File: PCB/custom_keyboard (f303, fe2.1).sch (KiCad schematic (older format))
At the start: 424 parts, among them IC1 FE2.1, J2 Conn_01x03_Male, J5 AVR-ISP-6, Q1 DTC123J, SW1 SW_Push, U1 24LC02BT-I/SN, U10 PRTR5V0U2X, U11 XC6206P332MR, U12 74LVC1G34, U13 XC6206P332MR, U2 PRTR5V0U2X, U3 PRTR5V0U2X, U4 PRTR5V0U2X, U5 PRTR5V0U2X, U6 PRTR5V0U2X, U7 PRTR5V0U2X, U8 PRTR5V0U2X, U9 STM32F303CBT6, Y1 8MHz, Y2 32.768KHz, Y3 12MHz

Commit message: Drew outlines for case
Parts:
- removed H2, H5: Hole, MountingHole:MountingHole_3.2mm_M3_Pad, symbol Mechanical:MountingHole_Pad
- J2: footprint Connector_JST:JST_GH_SM03B-GHS-TB_1x03-1MP_P1.25mm_Horizontal -> Connector_JST:JST_SH_SM03B-SRSS-TB_1x03-1MP_P1.00mm_Horizontal
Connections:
- net KEYBOARD_D+: now also R44.1, U9.33 (PA12)
- net KEYBOARD_D-: now also R43.1, U9.32 (PA11)
- net D-: now reaches R3.2, U3.3 (IO2), USB5.5 (DN2), USB5.7 (DN1)
- net D-: now also R2.1, R20.1, R25.1, R31.1, R37.1, R46.1, U10.3 (IO2), U2.3 (IO2), U4.3 (IO2), U5.3 (IO2), U6.3 (IO2), U7.3 (IO2), USB1.5 (DN2), USB1.7 (DN1), USB2.5 (DN2), USB2.7 (DN1), USB3.2 (D-), USB4.2 (D-), USB6.2 (D-), USB7.5 (DN2), USB7.7 (DN1)
- net D+: now reaches R6.2, U3.2 (IO1), USB5.6 (DP1), USB5.8 (DP2)
- net D+: now also R19.1, R24.1, R33.1, R34.1, R4.1, R45.1, U10.2 (IO1), U2.2 (IO1), U4.2 (IO1), U5.2 (IO1), U6.2 (IO1), U7.2 (IO1), USB1.6 (DP1), USB1.8 (DP2), USB2.6 (DP1), USB2.8 (DP2), USB3.3 (D+), USB4.3 (D+), USB6.3 (D+), USB7.6 (DP1), USB7.8 (DP2)
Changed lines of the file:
@@
 	0    -1   -1   0
 $EndComp
-Text GLabel 7550 18650 2    50   Input ~ 0
-KEYBOARD_D+
 Text GLabel 7550 18550 2    50   Input ~ 0
 KEYBOARD_D-
@@
 F 0 "J2" H 7108 16581 50  0000 C CNN
 F 1 "Conn_01x03_Male" H 7108 16490 50  0000 R CNN
-F 2 "Connector_JST:JST_GH_SM03B-GHS-TB_1x03-1MP_P1.25mm_Horizontal" H 7000 16300 50  0001 C CNN
+F 2 "Connector_JST:JST_SH_SM03B-SRSS-TB_1x03-1MP_P1.00mm_Horizontal" H 7000 16300 50  0001 C CNN
 F 3 "~" H 7000 16300 50  0001 C CNN
 	1    7000 16300
@@
 $EndComp
 $Comp
-L Mechanical:MountingHole_Pad H5
-U 1 1 6FB1C97B
-P 14550 21250
-F 0 "H5" H 14650 21299 50  0000 L CNN
-F 1 "Hole" H 14650 21208 50  0000 L CNN
-F 2 "MountingHole:MountingHole_3.2mm_M3_Pad" H 14550 21250 50  0001 C CNN
-F 3 "~" H 14550 21250 50  0001 C CNN
-	1    14550 21250
-	1    0    0    -1
-$EndComp
-$Comp
 L Mechanical:MountingHole_Pad H6
 U 1 1 6FB1CEC9
@@
 	14150 21450 14150 21350
 Wire Wire Line
-	14550 21350 14550 21450
-Wire Wire Line
 	14950 21350 14950 21450
 $Comp
@@
 $EndComp
 $Comp
-L Mechanical:MountingHole_Pad H2
-U 1 1 72E561AB
-P 13350 21250
-F 0 "H2" H 13450 21299 50  0000 L CNN
-F 1 "Hole" H 13450 21208 50  0000 L CNN
-F 2 "MountingHole:MountingHole_3.2mm_M3_Pad" H 13350 21250 50  0001 C CNN
-F 3 "~" H 13350 21250 50  0001 C CNN
-	1    13350 21250
-	1    0    0    -1
-$EndComp
-$Comp
 L Mechanical:MountingHole_Pad H3
 U 1 1 72E561B5
@@
 	12950 21450 12950 21350
 Wire Wire Line
-	13350 21350 13350 21450
-Wire Wire Line
 	13750 21350 13750 21450
-Wire Wire Line
-	12950 21450 13350 21450
 Connection ~ 14950 21450
-Connection ~ 13350 21450
-Wire Wire Line
-	13350 21450 13750 21450
 Connection ~ 13750 21450
 Wire Wire Line
@@
 Connection ~ 14150 21450
 Wire Wire Line
-	14150 21450 14550 21450
-Connection ~ 14550 21450
-Wire Wire Line
-	14550 21450 14950 21450
-Wire Wire Line
 	28050 3850 27950 3850
 Connection ~ 27950 3850
@@
 Wire Wire Line
 	10900 13200 10900 13500
+Text GLabel 22650 16250 1    50   Input ~ 0
+D+
+Text GLabel 22650 16350 3    50   Input ~ 0
+D-
+Text GLabel 22650 14300 3    50   Input ~ 0
+D-
+Text GLabel 22650 12250 3    50   Input ~ 0
+D-
+Text GLabel 22650 14200 1    50   Input ~ 0
+D+
+Text GLabel 22650 12150 1    50   Input ~ 0
+D+
+Text GLabel 26900 12300 1    50   Input ~ 0
+D-
+Text GLabel 26900 12400 3    50   Input ~ 0
+D+
+Text GLabel 26850 14850 3    50   Input ~ 0
+D+
+Text GLabel 26850 17300 3    50   Input ~ 0
+D+
+Text GLabel 26850 14750 1    50   Input ~ 0
+D-
+Text GLabel 26850 17200 1    50   Input ~ 0
+D-
+Text GLabel 14600 11950 3    50   Input ~ 0
+D+
+Text GLabel 14600 11850 1    50   Input ~ 0
+D-
+Text GLabel 7550 18650 2    50   Input ~ 0
+KEYBOARD_D+
+Text GLabel 7050 18650 3    50   Input ~ 0
+KEYBOARD_D+
+Text GLabel 7100 18550 1    50   Input ~ 0
+KEYBOARD_D-
+Wire Wire Line
+	12950 21450 13750 21450
+Wire Wire Line
+	14150 21450 14950 21450
 $EndSCHEMATC

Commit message: Draft 1-2
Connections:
- net KEYBOARD_D+: no longer R44.1, U9.33 (PA12)
- net KEYBOARD_D-: no longer R43.1, U9.32 (PA11)
- removed net D+: R19.1, R24.1, R33.1, R34.1, R4.1, R45.1, R6.2, U10.2 (IO1), U2.2 (IO1), U3.2 (IO1), U4.2 (IO1), U5.2 (IO1), U6.2 (IO1), U7.2 (IO1), USB1.6 (DP1), USB1.8 (DP2), USB2.6 (DP1), USB2.8 (DP2), USB3.3 (D+), USB4.3 (D+), USB5.6 (DP1), USB5.8 (DP2), USB6.3 (D+), USB7.6 (DP1), USB7.8 (DP2)
- removed net D-: R2.1, R20.1, R25.1, R3.2, R31.1, R37.1, R46.1, U10.3 (IO2), U2.3 (IO2), U3.3 (IO2), U4.3 (IO2), U5.3 (IO2), U6.3 (IO2), U7.3 (IO2), USB1.5 (DN2), USB1.7 (DN1), USB2.5 (DN2), USB2.7 (DN1), USB3.2 (D-), USB4.2 (D-), USB5.5 (DN2), USB5.7 (DN1), USB6.2 (D-), USB7.5 (DN2), USB7.7 (DN1)
- new net: R3.2, U3.3 (IO2), USB5.5 (DN2), USB5.7 (DN1)
- new net: R6.2, U3.2 (IO1), USB5.6 (DP1), USB5.8 (DP2)
- new net: R19.1, U4.2 (IO1), USB7.6 (DP1), USB7.8 (DP2)
- new net: R20.1, U4.3 (IO2), USB7.5 (DN2), USB7.7 (DN1)
- new net: R33.1, U6.2 (IO1), USB2.6 (DP1), USB2.8 (DP2)
- new net: R31.1, U6.3 (IO2), USB2.5 (DN2), USB2.7 (DN1)
- new net: R24.1, U5.2 (IO1), USB6.3 (D+)
- new net: R25.1, U5.3 (IO2), USB6.2 (D-)
- new net: R34.1, U7.2 (IO1), USB3.3 (D+)
- new net: R37.1, U7.3 (IO2), USB3.2 (D-)
- new net: R45.1, U10.2 (IO1), USB4.3 (D+)
- new net: R46.1, U10.3 (IO2), USB4.2 (D-)
- new net: R43.1, U9.32 (PA11)
- new net: R44.1, U9.33 (PA12)
- new net: R2.1, U2.3 (IO2), USB1.5 (DN2), USB1.7 (DN1)
- new net: R4.1, U2.2 (IO1), USB1.6 (DP1), USB1.8 (DP2)
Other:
- note added: "USB C Outputs"
- note removed: "USB C Outputs (5-7)"
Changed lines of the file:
@@
 Text GLabel 4250 3850 2    50   Input ~ 0
 ROT1_COL
-Text Notes 4550 3300 0    315  ~ 0
+Text Notes 4650 3200 0    315  ~ 0
 0
-Text Notes 6350 3300 0    315  ~ 0
+Text Notes 6100 3250 0    315  ~ 0
 1
-Text Notes 7700 3300 0    315  ~ 0
+Text Notes 7500 3250 0    315  ~ 0
 2
-Text Notes 3500 4050 0    315  ~ 0
-0
-Text Notes 3500 5050 0    315  ~ 0
+Text Notes 3350 5000 0    315  ~ 0
 1
-Text Notes 3500 6050 0    315  ~ 0
+Text Notes 3350 6000 0    315  ~ 0
 2
-Text Notes 3500 7050 0    315  ~ 0
+Text Notes 3350 7000 0    315  ~ 0
 3
-Text Notes 3500 8050 0    315  ~ 0
+Text Notes 3350 8000 0    315  ~ 0
 4
 Wire Wire Line
@@
 Text GLabel 8350 3100 1    50   Input ~ 0
 COL3
-Text Notes 11850 3300 0    315  ~ 0
+Text Notes 11750 3250 0    315  ~ 0
 5
-Text Notes 10450 3300 0    315  ~ 0
+Text Notes 10300 3250 0    315  ~ 0
 4
-Text Notes 9100 3300 0    315  ~ 0
+Text Notes 8900 3250 0    315  ~ 0
 3
 $Comp
@@
 Wire Wire Line
 	5300 4750 5300 4850
-Text Notes 13250 3300 0    315  ~ 0
+Text Notes 13100 3250 0    315  ~ 0
 6
-Text Notes 14700 3300 0    315  ~ 0
+Text Notes 14500 3250 0    315  ~ 0
 7
-Text Notes 16100 3300 0    315  ~ 0
+Text Notes 15900 3250 0    315  ~ 0
 8
-Text Notes 17450 3300 0    315  ~ 0
+Text Notes 17300 3250 0    315  ~ 0
 9
-Text Notes 18700 3300 0    315  ~ 0
+Text Notes 18550 3250 0    315  ~ 0
 10
-Text Notes 20100 3300 0    315  ~ 0
+Text Notes 20000 3250 0    315  ~ 0
 11
-Text Notes 21500 3300 0    315  ~ 0
+Text Notes 21350 3250 0    315  ~ 0
 12
-Text Notes 22900 3300 0    315  ~ 0
+Text Notes 22750 3250 0    315  ~ 0
 13
-Text Notes 24300 3300 0    315  ~ 0
+Text Notes 24150 3250 0    315  ~ 0
 14
 Text GLabel 16750 3100 1    50   Input ~ 0
@@
 Wire Wire Line
 	28550 4150 28550 4250
-Text Notes 28200 3300 0    315  ~ 0
+Text Notes 28400 3200 0    315  ~ 0
 17
-Text Notes 27100 3300 0    315  ~ 0
+Text Notes 26950 3250 0    315  ~ 0
 16
-Text Notes 25700 3300 0    315  ~ 0
+Text Notes 25550 3250 0    315  ~ 0
 15
 Text GLabel 28050 3850 2    50   Input ~ 0
@@
 Wire Wire Line
 	4150 7650 4150 6650
-Text Notes 3500 9050 0    315  ~ 0
+Text Notes 3350 9000 0    315  ~ 0
 5
 Text GLabel 4050 4850 0    50   Input ~ 0
@@
 Text GLabel 28350 17200 2    50   Input ~ 0
 HUB_PORT7_D-
-Text Notes 28300 11100 2    118  ~ 24
-USB C Outputs (5-7)
+Text Notes 28100 11150 2    118  ~ 24
+USB C Outputs
 Text Notes 21350 11500 0    79   ~ 0
 USB Output 3\n
@@
 Wire Wire Line
 	10900 13200 10900 13500
-Text GLabel 22650 16250 1    50   Input ~ 0
-D+
-Text GLabel 22650 16350 3    50   Input ~ 0
-D-
-Text GLabel 22650 14300 3    50   Input ~ 0
-D-
-Text GLabel 22650 12250 3    50   Input ~ 0
-D-
-Text GLabel 22650 14200 1    50   Input ~ 0
-D+
-Text GLabel 22650 12150 1    50   Input ~ 0
-D+
-Text GLabel 26900 12300 1    50   Input ~ 0
-D-
-Text GLabel 26900 12400 3    50   Input ~ 0
-D+
-Text GLabel 26850 14850 3    50   Input ~ 0
-D+
-Text GLabel 26850 17300 3    50   Input ~ 0
-D+
-Text GLabel 26850 14750 1    50   Input ~ 0
-D-
-Text GLabel 26850 17200 1    50   Input ~ 0
-D-
-Text GLabel 14600 11950 3    50   Input ~ 0
-D+
-Text GLabel 14600 11850 1    50   Input ~ 0
-D-
 Text GLabel 7550 18650 2    50   Input ~ 0
 KEYBOARD_D+
-Text GLabel 7050 18650 3    50   Input ~ 0
-KEYBOARD_D+
-Text GLabel 7100 18550 1    50   Input ~ 0
-KEYBOARD_D-
 Wire Wire Line
 	12950 21450 13750 21450
@@
 Wire Wire Line
 	9600 17200 9600 17000
+Text Notes 3350 4000 0    315  ~ 0
+0
 $EndSCHEMATC

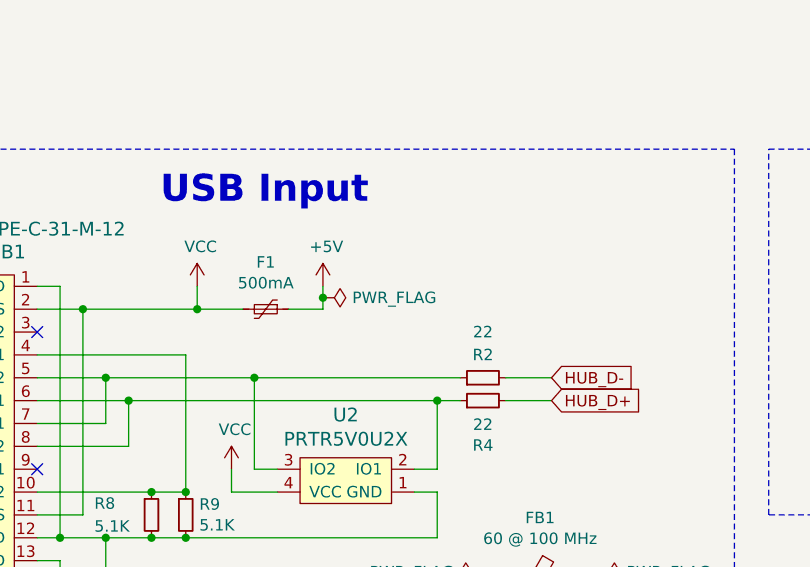
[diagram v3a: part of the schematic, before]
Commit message: Added a ferrite bead
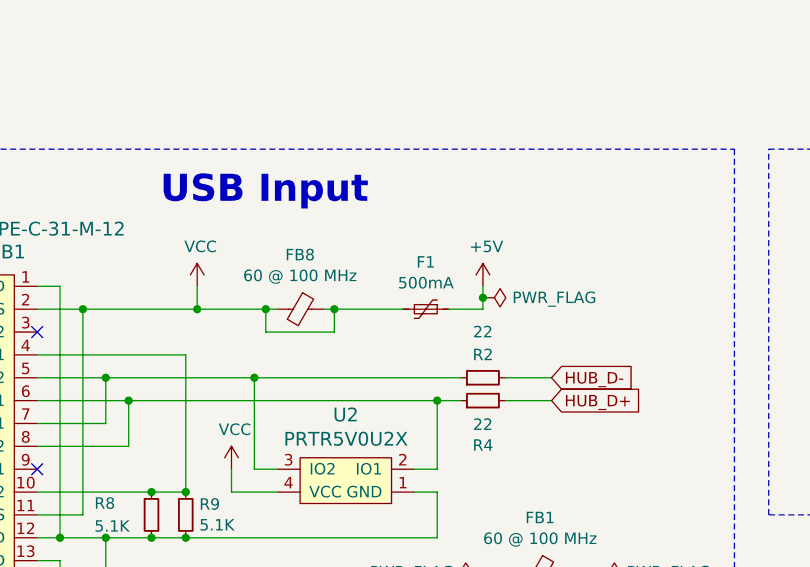
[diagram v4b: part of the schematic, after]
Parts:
- added FB8: 60 @ 100 MHz, Inductor_SMD:L_0805_2012Metric, symbol Device:Ferrite_Bead_Small
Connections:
- net +5V: now also FB8.1, FB8.2
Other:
- moved on the sheet: F1
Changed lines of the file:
@@
 	13950 12550 14150 12550
 $Comp
-L Device:Polyfuse_Small F1
-U 1 1 65C14F91
-P 14850 11550
-F 0 "F1" V 14645 11550 50  0000 C CNN
-F 1 "500mA" V 14736 11550 50  0000 C CNN
-F 2 "Fuse:Fuse_1206_3216Metric" H 14900 11350 50  0001 L CNN
-F 3 "~" H 14850 11550 50  0001 C CNN
-	1    14850 11550
-	0    1    1    0
-$EndComp
-$Comp
 L power:VCC #PWR091
 U 1 1 65C15E5C
@@
 L power:+5V #PWR092
 U 1 1 65C1A24C
-P 15100 11450
-F 0 "#PWR092" H 15100 11300 50  0001 C CNN
-F 1 "+5V" H 15115 11623 50  0000 C CNN
-F 2 "" H 15100 11450 50  0001 C CNN
-F 3 "" H 15100 11450 50  0001 C CNN
-	1    15100 11450
+P 15800 11450
+F 0 "#PWR092" H 15800 11300 50  0001 C CNN
+F 1 "+5V" H 15815 11623 50  0000 C CNN
+F 2 "" H 15800 11450 50  0001 C CNN
+F 3 "" H 15800 11450 50  0001 C CNN
+	1    15800 11450
 	1    0    0    -1
 $EndComp
-Wire Wire Line
-	15100 11550 14950 11550
-Wire Wire Line
-	14750 11550 14550 11550
 Connection ~ 14550 11550
 Wire Wire Line
@@
 Wire Wire Line
 	14550 11450 14550 11550
-$Comp
-L power:PWR_FLAG #FLG01
-U 1 1 E54A8F9E
-P 15100 11500
-F 0 "#FLG01" H 15100 11575 50  0001 C CNN
-F 1 "PWR_FLAG" V 15100 11628 50  0000 L CNN
-F 2 "" H 15100 11500 50  0001 C CNN
-F 3 "~" H 15100 11500 50  0001 C CNN
-	1    15100 11500
-	0    1    1    0
-$EndComp
-Wire Wire Line
-	15100 11450 15100 11500
-Wire Wire Line
-	15100 11500 15100 11550
-Connection ~ 15100 11500
 Wire Wire Line
 	17150 18650 17150 18850
@@
 Text Notes 3350 4000 0    315  ~ 0
 0
+Connection ~ 15800 11500
+Wire Wire Line
+	15800 11500 15800 11550
+Wire Wire Line
+	15800 11450 15800 11500
+$Comp
+L power:PWR_FLAG #FLG01
+U 1 1 E54A8F9E
+P 15800 11500
+F 0 "#FLG01" H 15800 11575 50  0001 C CNN
+F 1 "PWR_FLAG" V 15800 11628 50  0000 L CNN
+F 2 "" H 15800 11500 50  0001 C CNN
+F 3 "~" H 15800 11500 50  0001 C CNN
+	1    15800 11500
+	0    1    1    0
+$EndComp
+Wire Wire Line
+	15800 11550 15650 11550
+$Comp
+L Device:Ferrite_Bead_Small FB8
+U 1 1 6235F25C
+P 15000 11550
+F 0 "FB8" V 14763 11550 50  0000 C CNN
+F 1 "60 @ 100 MHz" V 14854 11550 50  0000 C CNN
+F 2 "Inductor_SMD:L_0805_2012Metric" V 14930 11550 50  0001 C CNN
+F 3 "~" H 15000 11550 50  0001 C CNN
+	1    15000 11550
+	0    1    1    0
+$EndComp
+$Comp
+L Device:Polyfuse_Small F1
+U 1 1 65C14F91
+P 15550 11550
+F 0 "F1" V 15345 11550 50  0000 C CNN
+F 1 "500mA" V 15436 11550 50  0000 C CNN
+F 2 "Fuse:Fuse_1206_3216Metric" H 15600 11350 50  0001 L CNN
+F 3 "~" H 15550 11550 50  0001 C CNN
+	1    15550 11550
+	0    1    1    0
+$EndComp
+Wire Wire Line
+	15100 11550 15150 11550
+Wire Wire Line
+	14550 11550 14850 11550
+Wire Wire Line
+	14850 11550 14850 11650
+Wire Wire Line
+	14850 11650 15150 11650
+Wire Wire Line
+	15150 11650 15150 11550
+Connection ~ 14850 11550
+Wire Wire Line
+	14850 11550 14900 11550
+Connection ~ 15150 11550
+Wire Wire Line
+	15150 11550 15450 11550
 $EndSCHEMATC

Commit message: Updated files, prepped for review
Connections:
- net KEYBOARD_D+: now also R44.1, U9.33 (PA12)
- net KEYBOARD_D-: now also R43.1, U9.32 (PA11)
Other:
- moved on the sheet: R42, R43, R44
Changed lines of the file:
@@
 L Device:R_Small R44
 U 1 1 83FFF6BA
-P 7250 18650
-F 0 "R44" V 7150 18750 50  0000 C CNN
-F 1 "22" V 7150 18550 50  0000 C CNN
-F 2 "Resistor_SMD:R_0805_2012Metric" H 7250 18650 50  0001 C CNN
-F 3 "~" H 7250 18650 50  0001 C CNN
-	1    7250 18650
-	0    -1   -1   0
+P 10600 17100
+F 0 "R44" V 10400 17100 50  0000 C CNN
+F 1 "22" V 10500 17100 50  0000 C CNN
+F 2 "Resistor_SMD:R_0805_2012Metric" H 10600 17100 50  0001 C CNN
+F 3 "~" H 10600 17100 50  0001 C CNN
+	1    10600 17100
+	0    -1   1    0
 $EndComp
 $Comp
 L Device:R_Small R43
 U 1 1 840036CC
-P 7250 18550
-F 0 "R43" V 7350 18650 50  0000 C CNN
-F 1 "22" V 7350 18450 50  0000 C CNN
-F 2 "Resistor_SMD:R_0805_2012Metric" H 7250 18550 50  0001 C CNN
-F 3 "~" H 7250 18550 50  0001 C CNN
-	1    7250 18550
+P 9400 17100
+F 0 "R43" V 9600 17100 50  0000 C CNN
+F 1 "22" V 9500 17100 50  0000 C CNN
+F 2 "Resistor_SMD:R_0805_2012Metric" H 9400 17100 50  0001 C CNN
+F 3 "~" H 9400 17100 50  0001 C CNN
+	1    9400 17100
 	0    -1   -1   0
 $EndComp
-Text GLabel 7550 18550 2    50   Input ~ 0
+Text GLabel 7350 18550 2    50   Input ~ 0
 KEYBOARD_D-
 Wire Wire Line
-	7450 18450 7450 18650
-Connection ~ 7450 18650
+	7250 18450 7250 18650
+Connection ~ 7250 18650
 $Comp
 L Device:R_Small R42
 U 1 1 8482A4BE
-P 7450 18350
-F 0 "R42" H 7509 18396 50  0000 L CNN
-F 1 "1.5k" H 7509 18305 50  0000 L CNN
-F 2 "Resistor_SMD:R_0805_2012Metric" H 7450 18350 50  0001 C CNN
-F 3 "~" H 7450 18350 50  0001 C CNN
-	1    7450 18350
+P 7250 18350
+F 0 "R42" H 7309 18396 50  0000 L CNN
+F 1 "1.5k" H 7309 18305 50  0000 L CNN
+F 2 "Resistor_SMD:R_0805_2012Metric" H 7250 18350 50  0001 C CNN
+F 3 "~" H 7250 18350 50  0001 C CNN
+	1    7250 18350
 	1    0    0    -1
 $EndComp
 Wire Wire Line
-	7450 18150 7450 18250
+	7250 18150 7250 18250
 $Comp
 L power:+5V #PWR0170
 U 1 1 6DAAD363
-P 7450 18150
-F 0 "#PWR0170" H 7450 18000 50  0001 C CNN
-F 1 "+5V" H 7465 18323 50  0000 C CNN
-F 2 "" H 7450 18150 50  0001 C CNN
-F 3 "" H 7450 18150 50  0001 C CNN
-	1    7450 18150
+P 7250 18150
+F 0 "#PWR0170" H 7250 18000 50  0001 C CNN
+F 1 "+5V" H 7265 18323 50  0000 C CNN
+F 2 "" H 7250 18150 50  0001 C CNN
+F 3 "" H 7250 18150 50  0001 C CNN
+	1    7250 18150
 	1    0    0    -1
 $EndComp
@@
 	7650 21050 7450 21050
 Wire Wire Line
-	7350 18550 7550 18550
-Wire Wire Line
-	7450 18650 7550 18650
-Text GLabel 10600 17100 2    50   Input ~ 0
+	7250 18650 7350 18650
+Text GLabel 10800 17100 2    50   Input ~ 0
 KEYBOARD_D+
-Text GLabel 9400 17100 0    50   Input ~ 0
-KEYBOARD_D-
 $Comp
 L power:GND #PWR0190
@@
 Wire Notes Line
 	8550 16450 11450 16450
-Wire Wire Line
-	7350 18650 7450 18650
-Wire Wire Line
-	6150 18550 7150 18550
-Wire Wire Line
-	6150 18650 7150 18650
 Text GLabel 6950 3100 1    50   Input ~ 0
 COL2
@@
 Wire Wire Line
 	10900 13200 10900 13500
-Text GLabel 7550 18650 2    50   Input ~ 0
+Text GLabel 7350 18650 2    50   Input ~ 0
 KEYBOARD_D+
 Wire Wire Line
@@
 	10400 17200 10300 17200
 Wire Wire Line
-	10300 17100 10600 17100
-Wire Wire Line
-	9400 17100 9700 17100
+	10300 17100 10450 17100
 Wire Wire Line
 	10400 17300 10400 17200
@@
 Wire Wire Line
 	15150 11550 15450 11550
+Wire Wire Line
+	6150 18550 7350 18550
+Wire Wire Line
+	6150 18650 7250 18650
+Text GLabel 9200 17100 0    50   Input ~ 0
+KEYBOARD_D-
+Wire Wire Line
+	9500 17100 9550 17100
+Wire Wire Line
+	10700 17100 10750 17100
+Wire Wire Line
+	10750 17100 10750 17200
+Wire Wire Line
+	10750 17200 10450 17200
+Wire Wire Line
+	10450 17200 10450 17100
+Connection ~ 10750 17100
+Wire Wire Line
+	10750 17100 10800 17100
+Connection ~ 10450 17100
+Wire Wire Line
+	10450 17100 10500 17100
+Wire Wire Line
+	9200 17100 9250 17100
+Wire Wire Line
+	9250 17100 9250 17200
+Wire Wire Line
+	9250 17200 9550 17200
+Wire Wire Line
+	9550 17200 9550 17100
+Connection ~ 9250 17100
+Wire Wire Line
+	9250 17100 9300 17100
+Connection ~ 9550 17100
+Wire Wire Line
+	9550 17100 9700 17100
 $EndSCHEMATC
